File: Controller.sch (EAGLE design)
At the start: 9 parts, among them IC1 74HCT04D, U1 CJT1117-3.3-SOT223

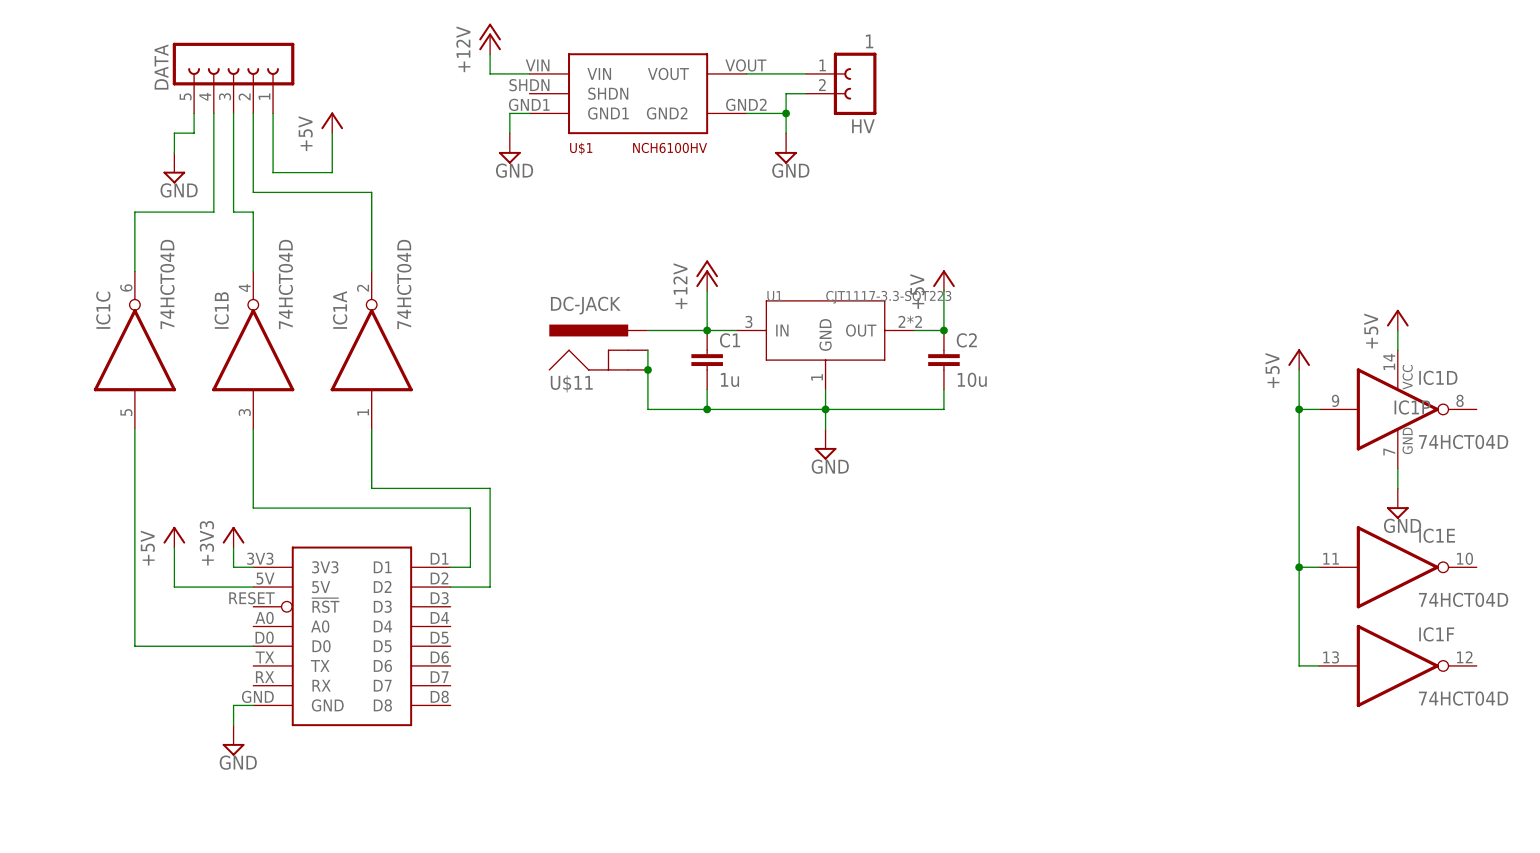
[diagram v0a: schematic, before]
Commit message: added second inverter stage to controller to have non-inverted logic on the outputs
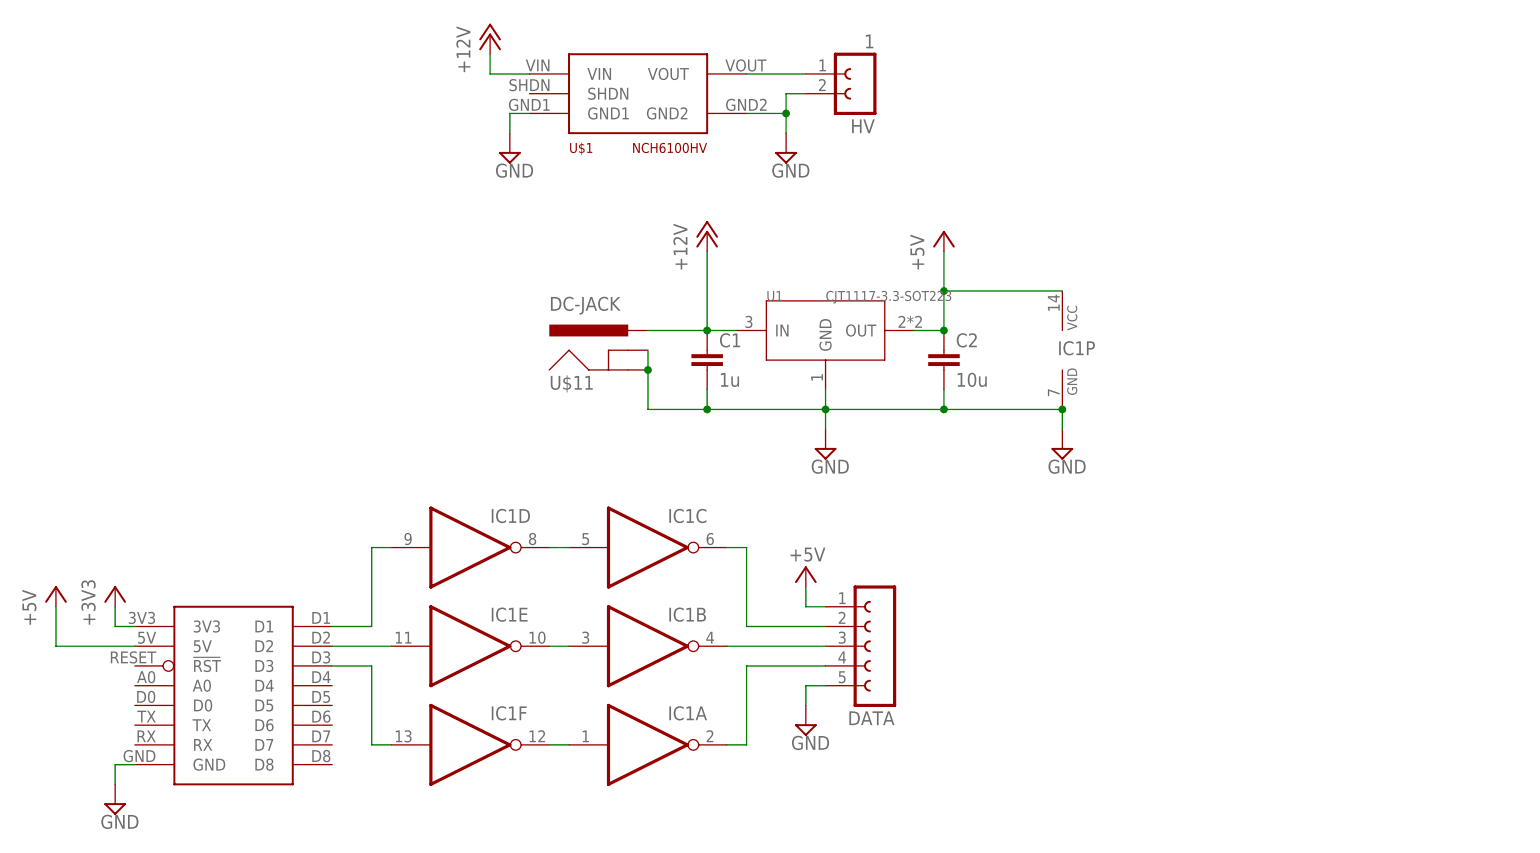
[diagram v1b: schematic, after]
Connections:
- removed net N$54: DATA.2, IC1A.O
- removed net N$61: IC1C.I, U$12.D0
- new net N$2: IC1C.I, IC1D.O
- new net N$3: IC1B.I, IC1E.O
- new net N$4: IC1A.I, IC1F.O
- new net N$7: IC1F.I, U$12.D3
- new net N$8: DATA.4, IC1A.O
- net +5V: no longer IC1D.I, IC1E.I, IC1F.I
- net N$60: now also DATA.2; no longer DATA.4
- net N$62: now also IC1D.I; no longer IC1B.I
- net N$63: now also IC1E.I; no longer IC1A.I
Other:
- moved on the sheet: DATA, IC1A, IC1B, IC1C, IC1D, IC1E, IC1F, IC1P
